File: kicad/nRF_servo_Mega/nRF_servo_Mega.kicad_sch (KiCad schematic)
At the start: 12 parts, among them J1 Screw_Terminal_01x02, M1 Motor_Servo, M2 Motor_Servo, M3 Motor_Servo, M4 Motor_Servo, M5 Motor_Servo, M6 Motor_Servo, U1 NRF24L01_Breakout

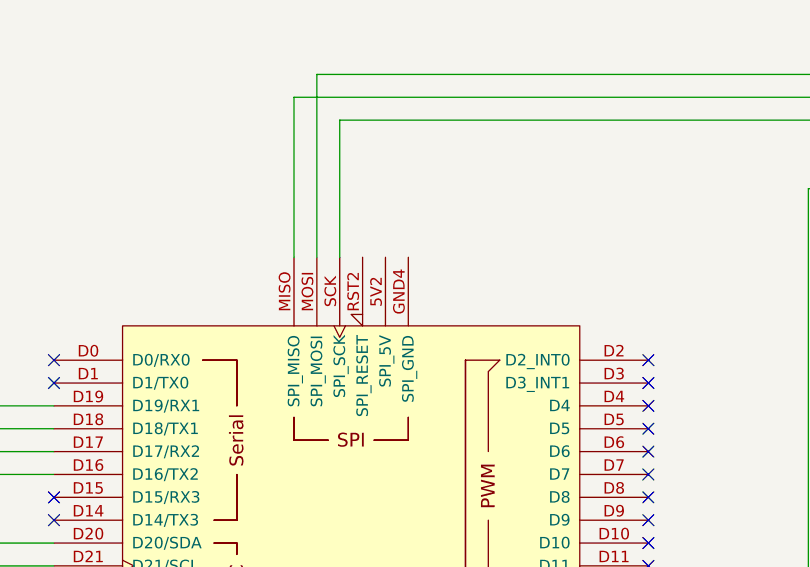
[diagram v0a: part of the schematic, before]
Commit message: rf24PerformingRobotsTemplate_2023 transmits and receives reliably
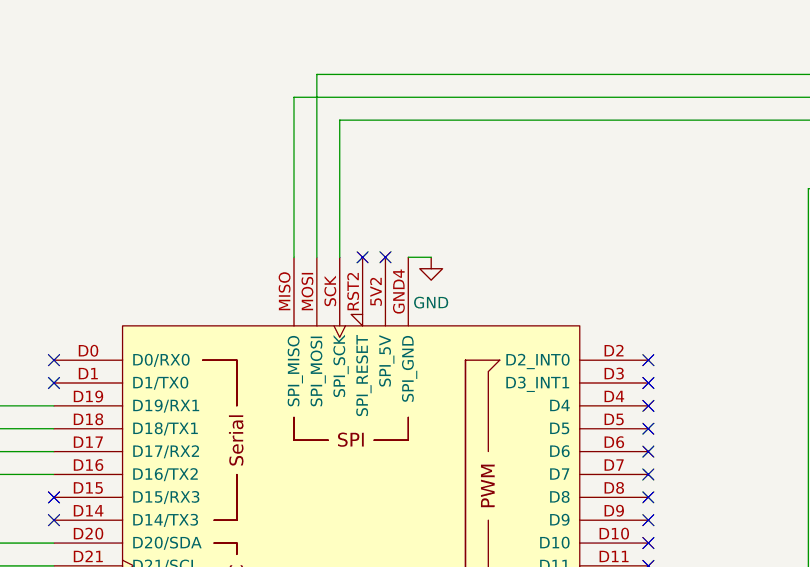
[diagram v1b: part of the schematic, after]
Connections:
- net GND: now also XA1.GND4 (SPI_GND)
- no-connect marks 72 -> 74
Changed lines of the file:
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@@
   (no_connect (at 171.45 114.3))
   (no_connect (at 171.45 101.6))
+  (no_connect (at 142.24 46.99))
   (no_connect (at 105.41 86.36))
   (no_connect (at 105.41 127))
@@
   (no_connect (at 105.41 73.66))
   (no_connect (at 105.41 104.14))
+  (no_connect (at 139.7 46.99))
   (no_connect (at 171.45 160.02))
   (no_connect (at 105.41 109.22))
@@
   )
   (wire (pts (xy 105.41 63.5) (xy 21.59 63.5))
+    (stroke (width 0) (type default))
+  )
+  (wire (pts (xy 144.78 46.99) (xy 147.32 46.99))
     (stroke (width 0) (type default))
   )
@@
         )
       )
+    )
+  )
+  (symbol (lib_id "power:GND") (at 147.32 46.99 0) (mirror y) (unit 1)
+    (in_bom yes) (on_board yes) (dnp no) (fields_autoplaced)
+    (property "Reference" "#PWR016" (at 147.32 53.34 0)
+      (effects (font (size 1.27 1.27)) hide)
+    )
+    (property "Value" "GND" (at 147.32 52.07 0)
+      (effects (font (size 1.27 1.27)))
+    )
+    (property "Footprint" "" (at 147.32 46.99 0)
+      (effects (font (size 1.27 1.27)) hide)
+    )
+    (property "Datasheet" "" (at 147.32 46.99 0)
+      (effects (font (size 1.27 1.27)) hide)
+    )
+    (pin "1")
+    (instances
+      (project "nRF_servo_Mega"
+        (path "/5d4ac997-0275-451c-a58a-d84421a0d8df"
+          (reference "#PWR016") (unit 1)
+        )
+      )

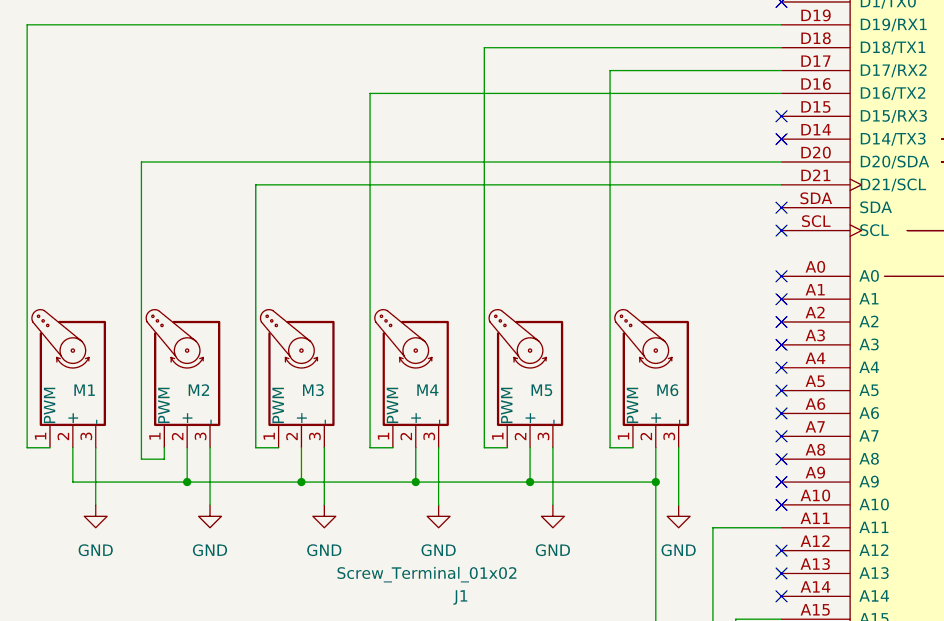
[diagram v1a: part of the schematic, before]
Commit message: finished hobby rc and motor controller shield
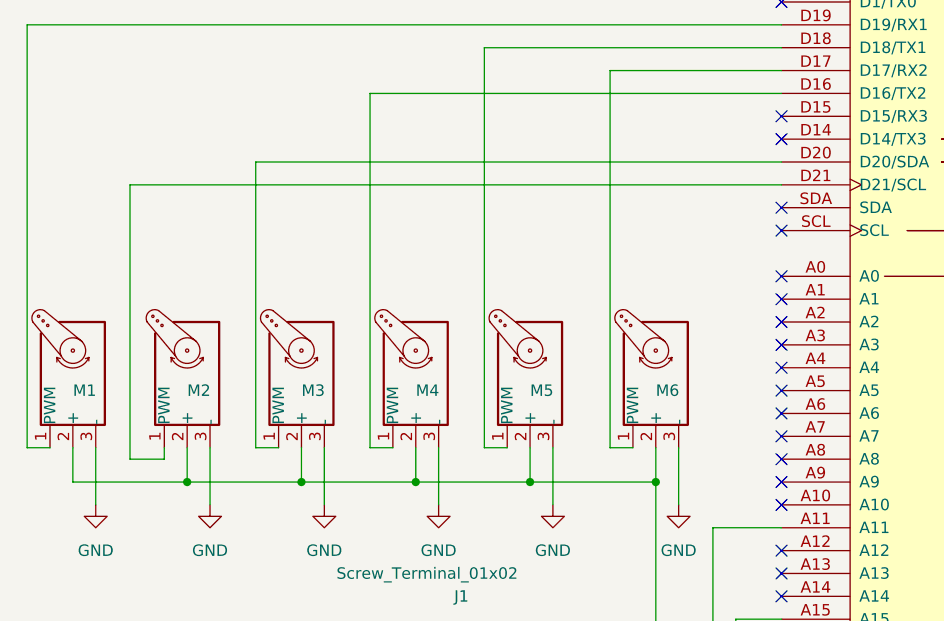
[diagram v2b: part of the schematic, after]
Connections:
- net at M2.1 (PWM): now also XA1.D21 (D21/SCL); no longer XA1.D20 (D20/SDA)
- net at M3.1 (PWM): now also XA1.D20 (D20/SDA); no longer XA1.D21 (D21/SCL)
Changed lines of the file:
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@@
-    (stroke (width 0) (type default))
-  )
-  (wire (pts (xy 105.41 81.28) (xy 46.99 81.28))
     (stroke (width 0) (type default))
   )
@@
     (stroke (width 0) (type default))
   )
-  (wire (pts (xy 34.29 78.74) (xy 105.41 78.74))
-    (stroke (width 0) (type default))
-  )
   (wire (pts (xy 41.91 110.49) (xy 41.91 116.84))
     (stroke (width 0) (type default))
@@
     (stroke (width 0) (type default))
   )
-  (wire (pts (xy 34.29 111.76) (xy 36.83 111.76))
+  (wire (pts (xy 33.02 111.76) (xy 36.83 111.76))
     (stroke (width 0) (type default))
   )
@@
   )
   (wire (pts (xy 39.37 114.3) (xy 52.07 114.3))
-    (stroke (width 0) (type default))
-  )
-  (wire (pts (xy 34.29 78.74) (xy 34.29 111.76))
     (stroke (width 0) (type default))
   )
@@
     (stroke (width 0) (type default))
   )
+  (wire (pts (xy 33.02 81.28) (xy 33.02 111.76))
+    (stroke (width 0) (type default))
+  )
   (wire (pts (xy 91.44 132.08) (xy 91.44 114.3))
     (stroke (width 0) (type default))
@@
     (stroke (width 0) (type default))
   )
-  (wire (pts (xy 46.99 110.49) (xy 46.99 81.28))
+  (wire (pts (xy 46.99 78.74) (xy 46.99 110.49))
     (stroke (width 0) (type default))
   )
@@
   )
   (wire (pts (xy 64.77 110.49) (xy 64.77 114.3))
+    (stroke (width 0) (type default))
+  )
+  (wire (pts (xy 46.99 78.74) (xy 105.41 78.74))
     (stroke (width 0) (type default))
   )
@@
     (stroke (width 0) (type default))
   )
+  (wire (pts (xy 33.02 81.28) (xy 105.41 81.28))
+    (stroke (width 0) (type default))
+  )
